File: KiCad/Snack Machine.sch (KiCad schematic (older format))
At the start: 42 parts, among them J1 RFID_CONNECTOR, J10 Row Screw Terminal, J11 Column Screw Terminal, J2 Power Screw Terminal, J5 MDB, J6 Conn_01x02, J7 LCD EXP1, J8 LCD EXP2, J9 AVR-ISP-6, Q1 P-CH 30V 3.8A, SW1 SW_SPST, U2 MEZD71202A-G, U3 ATmega2560-16AU, Y1 16MHz

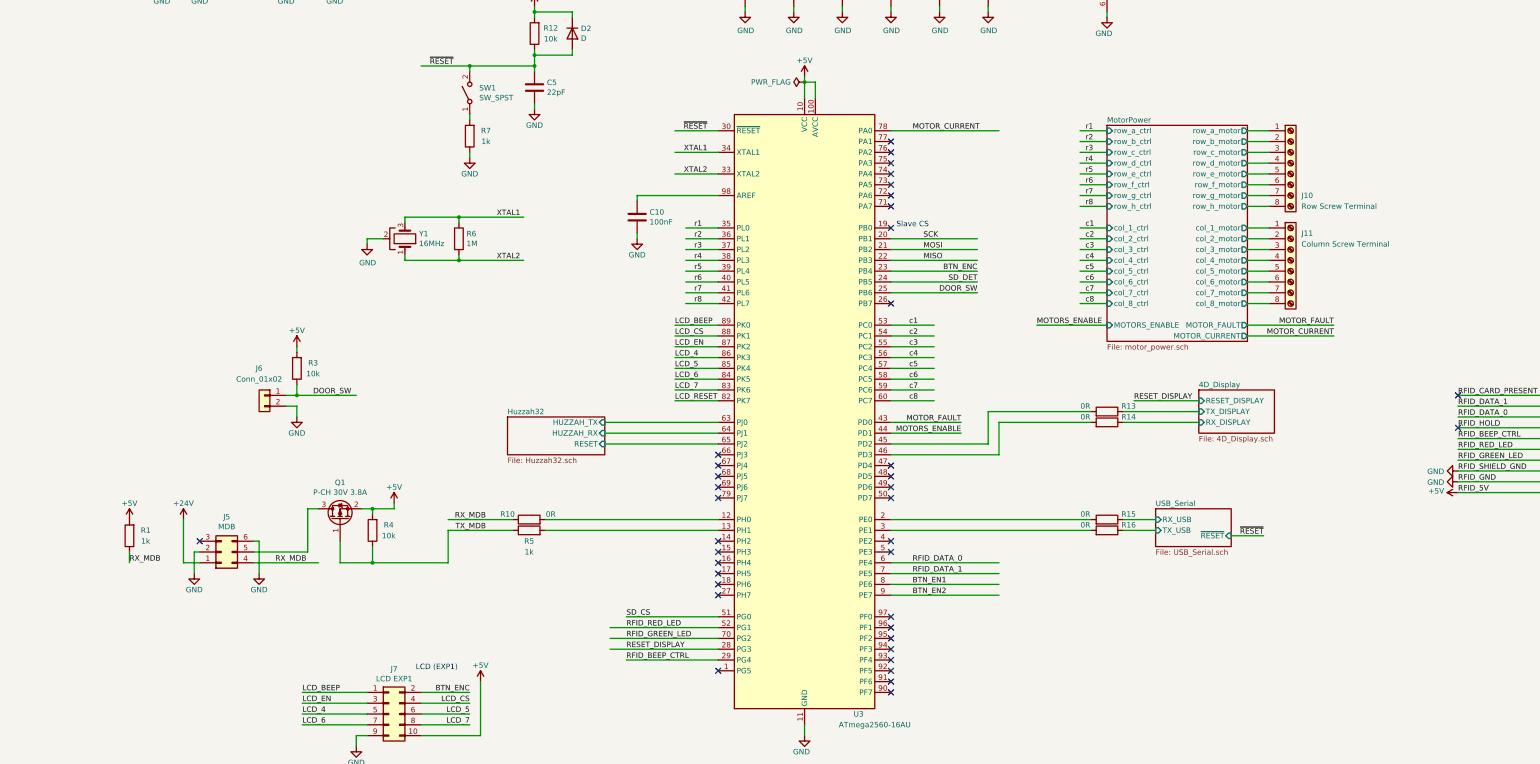
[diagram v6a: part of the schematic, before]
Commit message: Rotated serial ports around to make routing easier
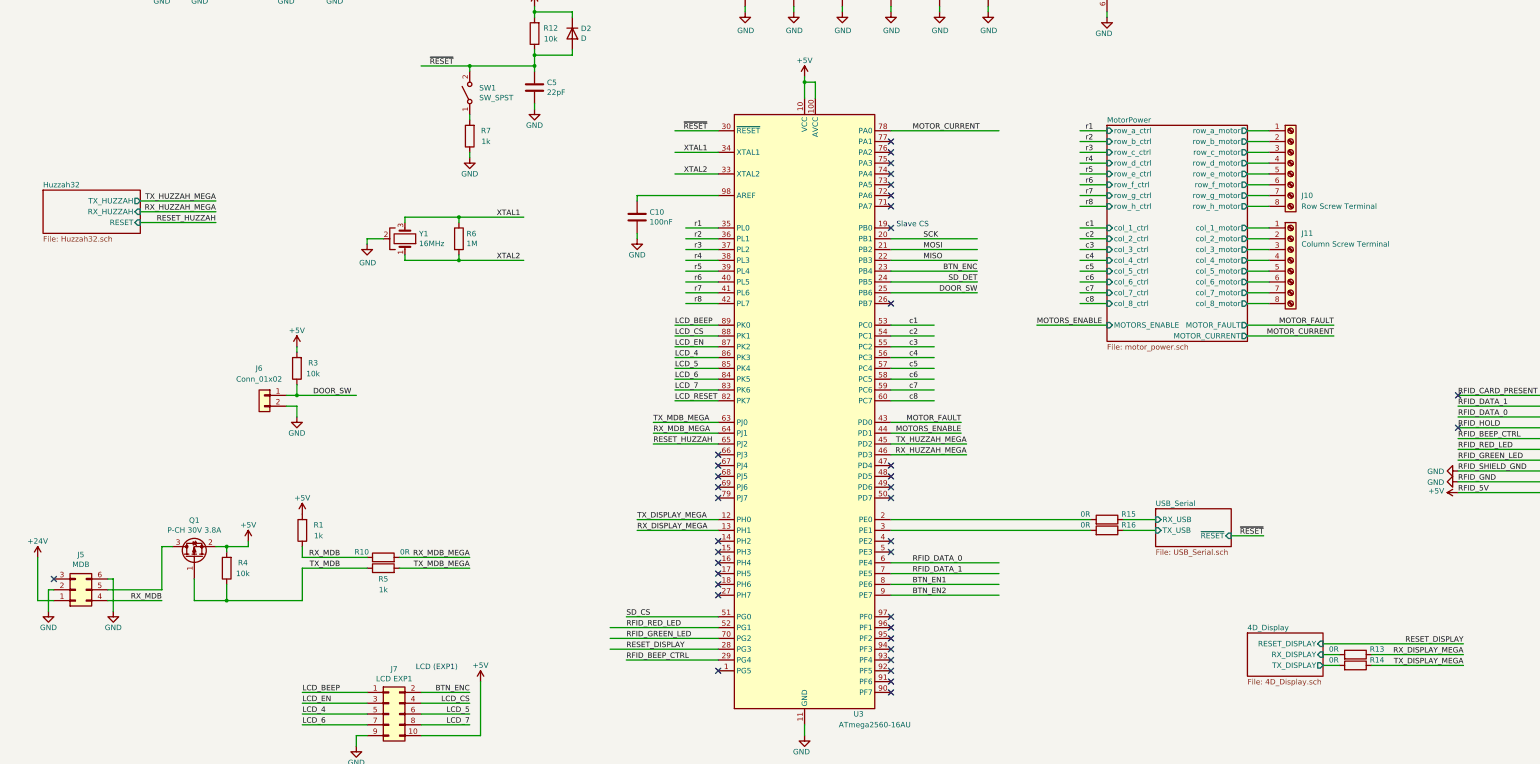
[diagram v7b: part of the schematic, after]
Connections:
- net labels added: RESET_HUZZAH, RX_DISPLAY_MEGA, RX_HUZZAH_MEGA, RX_MDB_MEGA, TX_DISPLAY_MEGA, TX_HUZZAH_MEGA, TX_MDB_MEGA
- wire segments 222 -> 225
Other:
- moved on the sheet: J5, Q1, R1, R10, R13, R14, R4, R5

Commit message: Unrouted is 0! Woot!
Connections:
- no-connect marks 40 -> 27
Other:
- note added: "This may not be an ADC pin we can use"
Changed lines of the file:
@@
 LCD_RESET
 NoConn ~ 4750 9650
-Text Label 6650 7800 0    50   ~ 0
-RESET_DISPLAY
-Wire Wire Line
-	7500 7800 6500 7800
 Text Label 12550 6750 2    50   ~ 0
 ~RESET
@@
 	9100 7300 10100 7300
 Text Label 9300 7200 0    50   ~ 0
+BTN_EN2
+Text Label 9300 7300 0    50   ~ 0
 BTN_EN1
-Text Label 9300 7300 0    50   ~ 0
-BTN_EN2
-Text Label 6650 7700 0    50   ~ 0
-RFID_GREEN_LED
-Text Label 6650 7600 0    50   ~ 0
-RFID_RED_LED
-Wire Wire Line
-	6500 7600 7500 7600
-Wire Wire Line
-	6500 7700 7500 7700
 $Comp
 L Connector_Generic:Conn_02x03_Top_Bottom J5
@@
 	4250 7050 3650 7050
 $Comp
-L MCU_Microchip_ATmega:ATmega2560-16AU U3
-U 1 1 5BFE17CA
-P 8300 5600
-F 0 "U3" H 8800 2800 50  0000 C CNN
-F 1 "ATmega2560-16AU" H 8950 2700 50  0000 C CNN
-F 2 "Package_QFP:TQFP-100_14x14mm_P0.5mm" H 8300 5600 50  0001 C CIN
-F 3 "http://ww1.microchip.com/downloads/en/DeviceDoc/Atmel-2549-8-bit-AVR-Microcontroller-ATmega640-1280-1281-2560-2561_datasheet.pdf" H 8300 5600 50  0001 C CNN
-	1    8300 5600
-	1    0    0    -1
-$EndComp
-$Comp
 L Device:R R15
 U 1 1 5C0D1512
@@
 Wire Wire Line
 	3650 7350 3650 7050
-Wire Wire Line
-	9100 4400 9900 4400
-Wire Wire Line
-	9100 4500 9900 4500
 $Comp
 L Connector_Generic:Conn_01x02 J6
@@
 SD_DET
 NoConn ~ 4250 9650
-Wire Wire Line
-	9100 4300 9900 4300
-Text Label 9900 4300 2    50   ~ 0
-BTN_ENC
 NoConn ~ 9100 3900
 Text Notes 9150 3900 0    50   ~ 0
 Slave CS
-Text Label 9900 4400 2    50   ~ 0
-SD_DET
 Wire Wire Line
 	7500 4800 7100 4800
 Text Label 7100 4800 0    50   ~ 0
 LCD_BEEP
-Wire Wire Line
-	7500 4900 7100 4900
-Text Label 7100 4900 0    50   ~ 0
-LCD_CS
-Wire Wire Line
-	7500 5000 7100 5000
-Text Label 7100 5000 0    50   ~ 0
-LCD_EN
-Wire Wire Line
-	7500 5100 7100 5100
-Text Label 7100 5100 0    50   ~ 0
-LCD_4
-Wire Wire Line
-	7500 5200 7100 5200
-Text Label 7100 5200 0    50   ~ 0
-LCD_5
-Wire Wire Line
-	7500 5300 7100 5300
-Text Label 7100 5300 0    50   ~ 0
-LCD_6
-Wire Wire Line
-	7500 5400 7100 5400
-Text Label 7100 5400 0    50   ~ 0
-LCD_7
-Text Label 9900 4500 2    50   ~ 0
-DOOR_SW
-Text Label 6650 7500 0    50   ~ 0
-SD_CS
-Wire Wire Line
-	6650 7500 7500 7500
 Wire Wire Line
 	9100 3000 10100 3000
@@
 $EndComp
 Connection ~ 3500 1650
-Text Label 7100 5500 0    50   ~ 0
-LCD_RESET
-Wire Wire Line
-	7100 5500 7500 5500
 NoConn ~ 9100 4600
 Text Label 9750 5700 2    50   ~ 0
 MOTOR_FAULT
 NoConn ~ 14350 5750
-Text Label 6650 7900 0    50   ~ 0
-RFID_BEEP_CTRL
-Wire Wire Line
-	6650 7900 7500 7900
 Text Label 9750 5800 2    50   ~ 0
 MOTORS_ENABLE
@@
 NoConn ~ 9100 6400
 NoConn ~ 7500 6000
-NoConn ~ 7500 6100
-NoConn ~ 7500 6200
-NoConn ~ 7500 6300
 NoConn ~ 7500 6400
-NoConn ~ 7500 6800
 NoConn ~ 7500 6900
 NoConn ~ 7500 7000
 NoConn ~ 7500 7100
-NoConn ~ 7500 7200
 NoConn ~ 7500 7300
 NoConn ~ 7500 8000
-NoConn ~ 9100 7500
-NoConn ~ 9100 7600
-NoConn ~ 9100 7700
-NoConn ~ 9100 7800
-NoConn ~ 9100 7900
-NoConn ~ 9100 8000
-NoConn ~ 9100 8100
-NoConn ~ 9100 8200
 NoConn ~ 9100 6800
 NoConn ~ 9100 6900
@@
 Wire Wire Line
 	2850 3850 2150 3850
-Text Label 6900 5900 0    50   ~ 0
-RESET_HUZZAH
-Wire Wire Line
-	6900 5900 7500 5900
 Text Label 9800 5900 2    50   ~ 0
 TX_HUZZAH_MEGA
@@
 Wire Wire Line
 	9800 6000 9100 6000
+Text Notes 9350 2900 0    50   ~ 0
+This may not be an ADC pin we can use
+Text Label 9550 7500 2    50   ~ 0
+LCD_RESET
+Wire Wire Line
+	9550 7500 9100 7500
+Text Label 9550 7600 2    50   ~ 0
+SD_CS
+Wire Wire Line
+	9550 7600 9100 7600
+Text Label 9550 7900 2    50   ~ 0
+LCD_6
+Wire Wire Line
+	9550 7700 9100 7700
+Text Label 9550 7700 2    50   ~ 0
+LCD_EN
+Text Label 9550 7800 2    50   ~ 0
+LCD_4
+Wire Wire Line
+	9550 7800 9100 7800
+Wire Wire Line
+	9550 7900 9100 7900
+Text Label 9550 8000 2    50   ~ 0
+LCD_7
+Wire Wire Line
+	9550 8000 9100 8000
+Text Label 9550 8100 2    50   ~ 0
+LCD_5
+Wire Wire Line
+	9100 8100 9550 8100
+Text Label 9550 8200 2    50   ~ 0
+LCD_CS
+Wire Wire Line
+	9550 8200 9100 8200
+Text Label 6850 4900 0    50   ~ 0
+RFID_GREEN_LED
+$Comp
+L MCU_Microchip_ATmega:ATmega2560-16AU U3
+U 1 1 5BFE17CA
+P 8300 5600
+F 0 "U3" H 8800 2800 50  0000 C CNN
+F 1 "ATmega2560-16AU" H 8950 2700 50  0000 C CNN
+F 2 "Package_QFP:TQFP-100_14x14mm_P0.5mm" H 8300 5600 50  0001 C CIN
+F 3 "http://ww1.microchip.com/downloads/en/DeviceDoc/Atmel-2549-8-bit-AVR-Microcontroller-ATmega640-1280-1281-2560-2561_datasheet.pdf" H 8300 5600 50  0001 C CNN
+	1    8300 5600
+	1    0    0    -1
+$EndComp
+Wire Wire Line
+	7500 4900 6850 4900
+Text Label 6850 5000 0    50   ~ 0
+RFID_RED_LED
+Text Label 6850 5100 0    50   ~ 0
+RFID_BEEP_CTRL
+Wire Wire Line
+	6850 5100 7500 5100
+Wire Wire Line
+	7500 5000 6850 5000
+Text Label 6750 6800 0    50   ~ 0
+RESET_DISPLAY
+Wire Wire Line
+	6750 6800 7500 6800
+Text Label 6900 6200 0    50   ~ 0
+SD_DET
+Wire Wire Line
+	6900 6200 7500 6200
+Text Label 6900 6300 0    50   ~ 0
+BTN_ENC
+Wire Wire Line
+	6900 6300 7500 6300
+Text Label 6900 6100 0    50   ~ 0
+DOOR_SW
+Wire Wire Line
+	7500 6100 6900 6100
+Text Label 6750 7200 0    50   ~ 0
+RESET_HUZZAH
+Wire Wire Line
+	6750 7200 7500 7200
 $EndSCHEMATC
